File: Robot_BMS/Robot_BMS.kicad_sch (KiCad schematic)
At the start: 62 parts, among them IC1 BQ34Z100PWR-R2, J1 USB_C_Receptacle_PowerOnly_24P, Q1 SIS413DN-T1-GE3, Q2 SIS413DN-T1-GE3, Q3 SIS413DN-T1-GE3, Q4 SIS413DN-T1-GE3, Q5 SIS413DN-T1-GE3, Q6 SIS413DN-T1-GE3, Q7 2N7002, Q8 2N7002, Q9 2N7002, U1 BQ297xy, U2 BQ297xy, U3 BQ297xy, U4 MCP73833-xxx-MF, U5 MCP73833-xxx-MF, U6 MCP73833-xxx-MF

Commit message: working on thee fuel gauge
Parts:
- added C10, C11: 0.1u, symbol Device:C
- added R22, R23: 10k, symbol Device:R
- added R24: 16k5, symbol Device:R
- added R25: 214k5, symbol Device:R
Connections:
- net +3.3V: now also IC1.5 (CE), IC1.6 (REGIN), C10.1, R22.2, R23.2
- net GND: now also BT3.2 (-), IC1.1 (P2), IC1.3 (P1), IC1.8 (VSS), Q5.1 (S_1), Q5.2 (S_2), Q5.3 (S_3), C10.2, C11.2, R24.1
- net -BATT: now reaches BT1.1 (+), C4.1, R5.1, U6.10 (V_{BAT}), U6.9 (V_{BAT})
- net -BATT: now also R25.2
- net SCL: now reaches IC1.13 (P4/SCL)
- net SCL: now also R23.1
- net SDA: now reaches IC1.14 (P3/SDA)
- net SDA: now also R22.1
- net at IC1.4 (BAT): now also C11.1, R24.2, R25.1
- no-connect marks 3 -> 7
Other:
- note added: "VOLSEL bit must be configured(set)for multicell operation Voltage Divider Network for Bat Pin: R = 16.5K(12.6V-0.9V)/0.9V = 214k5"
- moved on the sheet: BT1, BT2, BT3, C1, C2, C3, C4, C5, C6, C7, C8, C9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

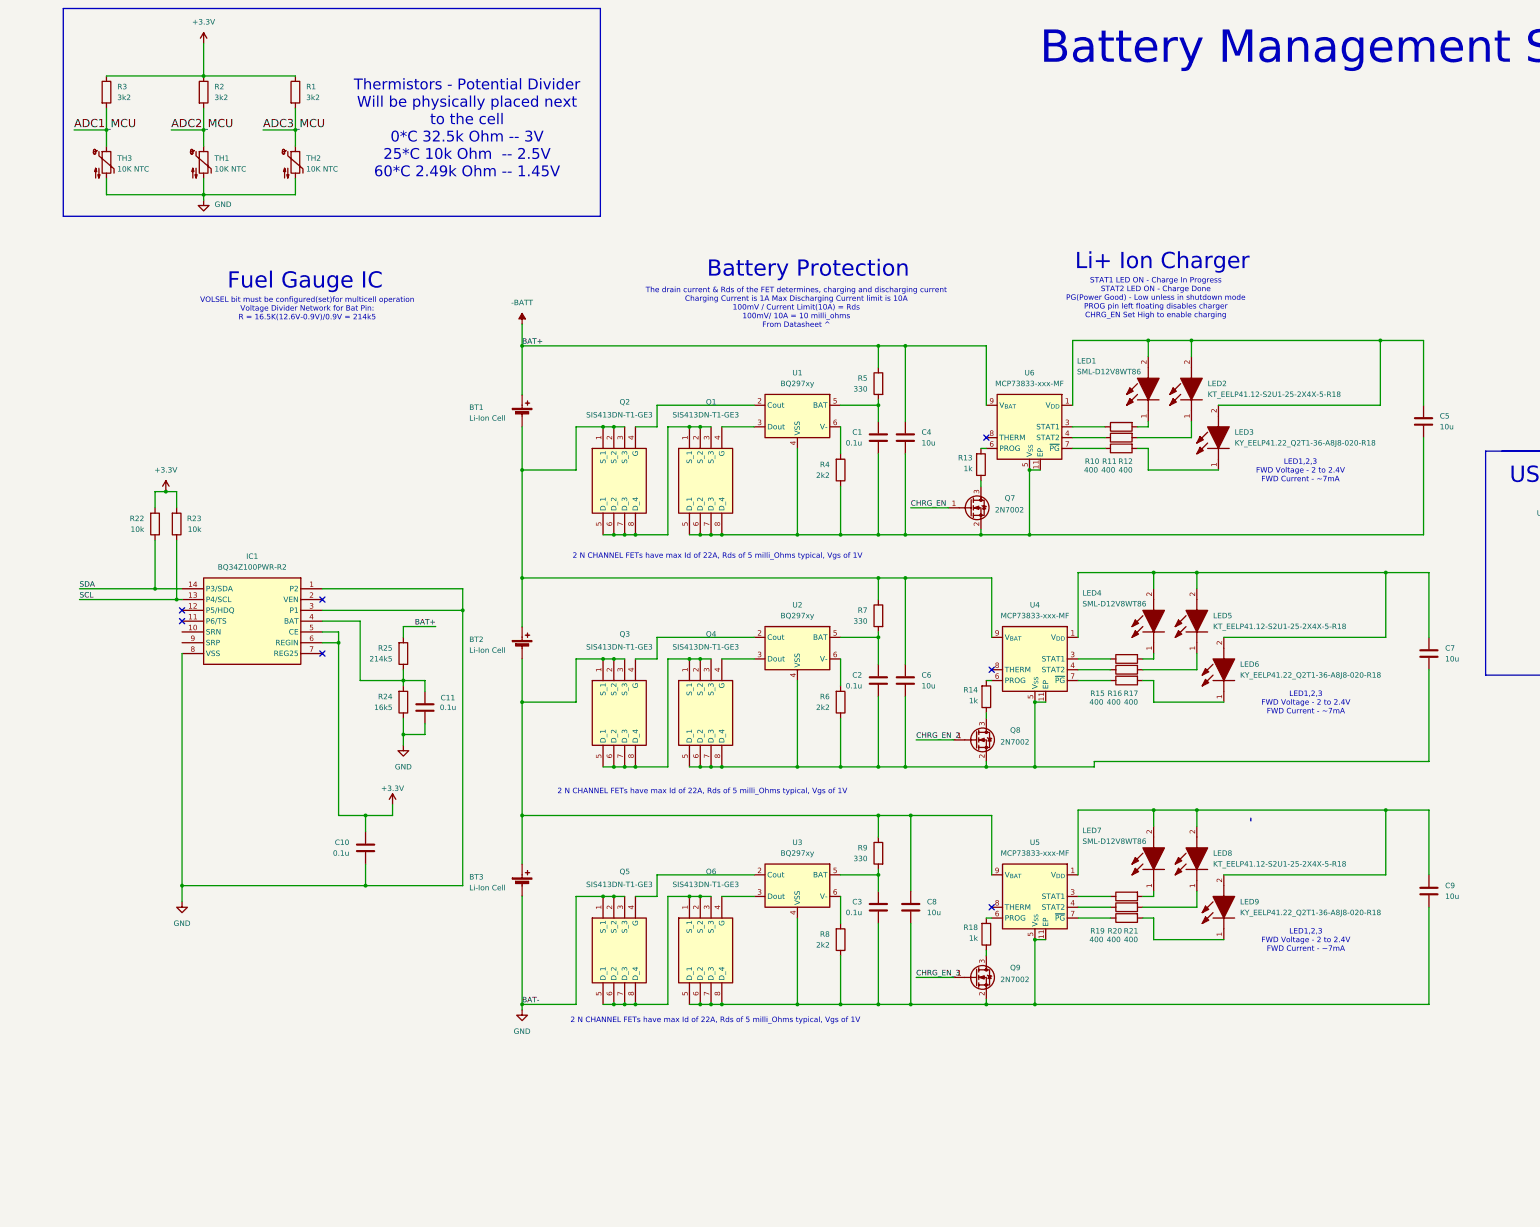
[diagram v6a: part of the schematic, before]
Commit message: implementing hierarchical schematics
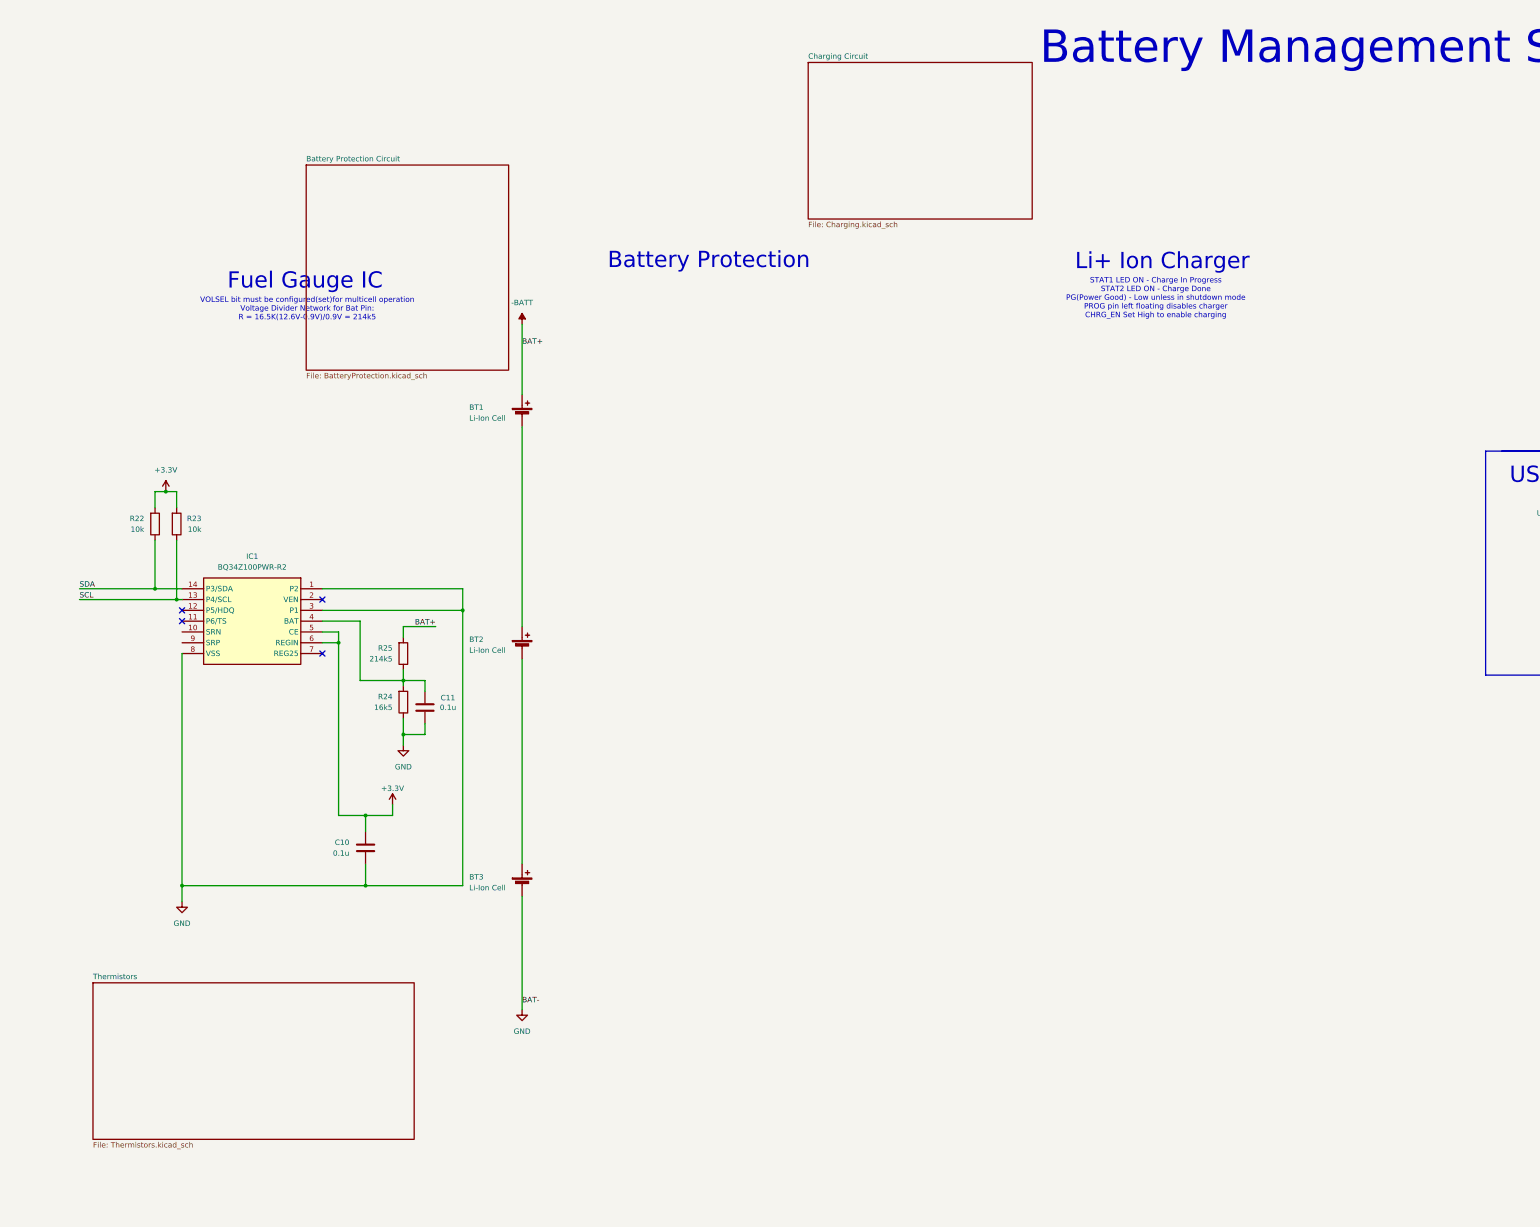
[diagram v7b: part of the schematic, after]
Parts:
- removed C1, C2, C3: 0.1u, symbol Device:C
- removed C4, C5, C6, C7, C8, C9: 10u, symbol Device:C
- removed LED1, LED4, LED7: SML-D12V8WT86, SMLD12V8WT86, symbol SML-D12V8WT86:SML-D12V8WT86
- removed LED2, LED5, LED8: KT_EELP41.12-S2U1-25-2X4X-5-R18, KTEELP4112S2U1252X4X5R18, symbol KT EELP41.12-S2U1-25-2X4X-5-R18:KT_EELP41.12-S2U1-25-2X4X-5-R18
- removed LED3, LED6, LED9: KY_EELP41.22_Q2T1-36-A8J8-020-R18, KYEELP4122Q2T136A8J8020R18, symbol KY EELP41.22 Q2T1-36-A8J8-020-R18:KY_EELP41.22_Q2T1-36-A8J8-020-R18
- removed Q1, Q2, Q3, Q4, Q5, Q6: SIS413DN-T1-GE3, SIS862DNT1GE3, symbol SIS413DN-T1-GE3:SIS413DN-T1-GE3
- removed Q7, Q8, Q9: 2N7002, Package_TO_SOT_SMD:SOT-23, symbol Transistor_FET:2N7002
- removed R1, R2, R3: 3k2, symbol Device:R
- removed R10, R11, R12, R15, R16, R17, R19, R20, R21: 400, symbol Device:R
- removed R13, R14, R18: 1k, symbol Device:R
- removed R4, R6, R8: 2k2, symbol Device:R
- removed R5, R7, R9: 330, symbol Device:R
- removed TH1, TH2, TH3: 10K NTC, symbol Device:Thermistor_NTC
- removed U1, U2, U3: BQ297xy, Package_SON:WSON-6_1.5x1.5mm_P0.5mm, symbol Battery_Management:BQ297xy
- removed U4, U5, U6: MCP73833-xxx-MF, Package_DFN_QFN:DFN-10-1EP_3x3mm_P0.5mm_EP1.58x2.35mm, symbol Battery_Management:MCP73833-xxx-MF
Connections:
- no-connect marks 7 -> 4
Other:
- added sheet Battery Protection Circuit (BatteryProtection.kicad_sch)
- added sheet Charging Circuit (Charging.kicad_sch)
- added sheet Thermistors (Thermistors.kicad_sch)
- note removed: "2 N CHANNEL FETs have max Id of 22A, Rds of 5 milli_Ohms typical, Vgs of 1V"
- note removed: "LED1,2,3 FWD Voltage - 2 to 2.4V FWD Current - ~7mA"
- note removed: "The drain current & Rds of the FET determines, charging and discharging current Charging Current is 1A Max Discharging Current limit is 10A 100mV / Current Limit(10A) = Rds 100mV/ 10A = 10 milli_ohms From Datasheet ^"
- note removed: "Thermistors - Potential Divider Will be physically placed next to the cell 0*C 32.5k Ohm -- 3V 25*C 10k Ohm -- 2.5V 60*C 2.49k Ohm -- 1.45V"

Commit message: cleaning up hierarchical schematics
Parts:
- removed BT1, BT2, BT3: Li-Ion Cell, symbol Device:Battery_Cell
- removed C10, C11: 0.1u, symbol Device:C
- removed IC1: BQ34Z100PWR-R2, SOP65P640X120-14N, symbol BQ34Z100PWR-R2:BQ34Z100PWR-R2
- removed J1: USB_C_Receptacle_PowerOnly_24P, symbol Connector:USB_C_Receptacle_PowerOnly_24P
- removed R22, R23: 10k, symbol Device:R
- removed R24: 16k5, symbol Device:R
- removed R25: 214k5, symbol Device:R
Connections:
- no-connect marks 4 -> 0
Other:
- added sheet Battery (BatteryConnectors.kicad_sch)
- added sheet Fuel Gauge (FuelGauge.kicad_sch)
- added sheet To MCU (MCUConnections.kicad_sch)
- added sheet USB-C (USBC.kicad_sch)
- sheet Battery Protection Circuit ports: added CELL_1+, CELL_1-, CELL_2+, CELL_2-, CELL_3+, CELL_3-; removed none
- sheet Charging Circuit ports: added CELL_1+, CELL_1-, CELL_2+, CELL_2-, CELL_3+, CELL_3-; removed none
- sheet Thermistors ports: added ADC1_MCU, ADC2_MCU, ADC3_MCU; removed none
- note removed: "Battery Protection"
- note removed: "Fuel Gauge IC"
- note removed: "Li+ Ion Charger"
- note removed: "STAT1 LED ON - Charge In Progress STAT2 LED ON - Charge Done PG(Power Good) - Low unless in shutdown mode PROG pin left floating disables charger CHRG_EN Set High to enable charging"
- note removed: "USB-C Connector"
- note removed: "VOLSEL bit must be configured(set)for multicell operation Voltage Divider Network for Bat Pin: R = 16.5K(12.6V-0.9V)/0.9V = 214k5"
